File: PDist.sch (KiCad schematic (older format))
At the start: 2 parts

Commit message: Upgrade FPGA size, re-route SDRAM
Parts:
- removed BRIDGE1: XC6SLX25-CSG324, manuf:XILINX-CSG324, symbol XC6SLX25-CSG324
- added BRIDGE1: XC6SLX25-FGG484, manuf:XILINX-FGG484, symbol XC6SLX25-FGG484
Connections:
- net labels added: VCCAUX, VCORE
- net labels removed: +1.2, +3.3
- wire segments 150 -> 163

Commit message: Uh, more misc work.
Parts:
- added LIMB1: LPC435xFET256, smd-semi:BGA100P1700X1700-256, symbol LPC435xFET256
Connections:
- net labels added: 3V3_LIMB
- wire segments 163 -> 208
- no-connect marks 0 -> 1
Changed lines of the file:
@@
 $Descr A4 11693 8268
 encoding utf-8
-Sheet 3 8
+Sheet 3 9
 Title ""
 Date ""
@@
 Wire Wire Line
 	6000 6900 6000 1000
+$Comp
+L LPC435xFET256 LIMB?
+U 1 1 577B6870
+P 9400 4700
+AR Path="/5765CB89/577B6870" Ref="LIMB?"  Part="2"
+AR Path="/5763AB3B/577B6870" Ref="LIMB1"  Part="1"
+F 0 "LIMB1" H 10431 3696 50  0000 L CNN
+F 1 "LPC435xFET256" H 10431 3605 50  0000 L CNN
+F 2 "smd-semi:BGA100P1700X1700-256" H 9400 5200 50  0001 C CNN
+F 3 "http://www.nxp.com/documents/data_sheet/LPC435X_3X_2X_1X.pdf" H 9400 5100 50  0001 C CNN
+	1    9400 4700
+	1    0    0    -1
+$EndComp
+$Comp
+L GND #PWR6
+U 1 1 577B6906
+P 9300 6900
+F 0 "#PWR6" H 9300 6900 30  0001 C CNN
+F 1 "GND" H 9300 6830 30  0001 C CNN
+F 2 "" H 9300 6900 60  0000 C CNN
+F 3 "" H 9300 6900 60  0000 C CNN
+	1    9300 6900
+	1    0    0    -1
+$EndComp
+Wire Wire Line
+	9300 4700 9400 4700
+Wire Wire Line
+	9300 4800 9400 4800
+Wire Wire Line
+	9300 4900 9400 4900
+Wire Wire Line
+	9300 5000 9400 5000
+Wire Wire Line
+	9300 5100 9400 5100
+Wire Wire Line
+	9300 5200 9400 5200
+Wire Wire Line
+	9300 5300 9400 5300
+Wire Wire Line
+	9300 5400 9400 5400
+Wire Wire Line
+	9300 5500 9400 5500
+Wire Wire Line
+	9300 5600 9400 5600
+Wire Wire Line
+	9300 5700 9400 5700
+Wire Wire Line
+	9300 5800 9400 5800
+Wire Wire Line
+	9300 5900 9400 5900
+Wire Wire Line
+	9300 6000 9400 6000
+Wire Wire Line
+	9300 6100 9400 6100
+Wire Wire Line
+	9300 6200 9400 6200
+Wire Wire Line
+	9300 6300 9400 6300
+Wire Wire Line
+	9300 6400 9400 6400
+Wire Wire Line
+	9300 6500 9400 6500
+Wire Wire Line
+	9300 6600 9400 6600
+Wire Wire Line
+	9300 6700 9400 6700
+Wire Wire Line
+	9300 6800 9400 6800
+Connection ~ 9300 4800
+Connection ~ 9300 4900
+Connection ~ 9300 5000
+Connection ~ 9300 5100
+Connection ~ 9300 5200
+Connection ~ 9300 5300
+Connection ~ 9300 5400
+Connection ~ 9300 5500
+Connection ~ 9300 5600
+Connection ~ 9300 5700
+Connection ~ 9300 5800
+Connection ~ 9300 5900
+Connection ~ 9300 6000
+Connection ~ 9300 6100
+Connection ~ 9300 6200
+Connection ~ 9300 6300
+Connection ~ 9300 6400
+Connection ~ 9300 6500
+Connection ~ 9300 6600
+Connection ~ 9300 6700
+Connection ~ 9300 6800
+Wire Wire Line
+	9300 4700 9300 6900
+$Comp
+L LPC435xFET256 LIMB?
+U 19 1 577B6DFB
+P 9400 2300
+AR Path="/5765CB89/577B6DFB" Ref="LIMB?"  Part="2"
+AR Path="/5763AB3B/577B6DFB" Ref="LIMB1"  Part="19"
+F 0 "LIMB1" H 10631 1296 50  0000 L CNN
+F 1 "LPC435xFET256" H 10631 1205 50  0000 L CNN
+F 2 "smd-semi:BGA100P1700X1700-256" H 9400 2800 50  0001 C CNN
+F 3 "http://www.nxp.com/documents/data_sheet/LPC435X_3X_2X_1X.pdf" H 9400 2700 50  0001 C CNN
+	19   9400 2300
+	1    0    0    -1
+$EndComp
+Wire Wire Line
+	9200 2300 9400 2300
+Wire Wire Line
+	9300 2400 9400 2400
+Wire Wire Line
+	9300 2500 9400 2500
+Wire Wire Line
+	9300 2600 9400 2600
+Wire Wire Line
+	9300 2700 9400 2700
+Wire Wire Line
+	9300 2800 9400 2800
+Wire Wire Line
+	9300 3000 9400 3000
+Wire Wire Line
+	9300 3100 9400 3100
+Wire Wire Line
+	9300 3200 9400 3200
+Wire Wire Line
+	9300 3300 9400 3300
+Wire Wire Line
+	9300 3400 9400 3400
+Wire Wire Line
+	9300 3500 9400 3500
+Wire Wire Line
+	9300 3600 9400 3600
+Wire Wire Line
+	9300 3700 9400 3700
+Wire Wire Line
+	9300 3800 9400 3800
+Wire Wire Line
+	9300 3900 9400 3900
+Wire Wire Line
+	9300 4000 9400 4000
+Wire Wire Line
+	9300 4100 9400 4100
+Wire Wire Line
+	9300 4200 9400 4200
+Wire Wire Line
+	9300 4300 9400 4300
+Wire Wire Line
+	9300 4400 9400 4400
+Connection ~ 9300 2300
+Connection ~ 9300 2400
+Connection ~ 9300 2500
+Connection ~ 9300 2600
+Connection ~ 9300 2700
+Connection ~ 9300 2800
+Connection ~ 9300 3000
+Connection ~ 9300 3100
+Connection ~ 9300 3200
+Connection ~ 9300 3300
+Connection ~ 9300 3400
+Connection ~ 9300 3500
+Connection ~ 9300 3600
+Connection ~ 9300 3700
+Connection ~ 9300 3800
+Connection ~ 9300 3900
+Connection ~ 9300 4000
+Connection ~ 9300 4100
+Connection ~ 9300 4200
+Connection ~ 9300 4300
+NoConn ~ 9400 2900
+Text GLabel 9200 2300 0    50   Input ~ 0
+3V3_LIMB
+Wire Wire Line
+	9300 2300 9300 4400
 $EndSCHEMATC

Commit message: MOAR WORK
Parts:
- removed LIMB1: LPC435xFET256, smd-semi:BGA100P1700X1700-256, symbol LPC435xFET256
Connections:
- net labels removed: 3V3_LIMB
- wire segments 208 -> 163
- no-connect marks 1 -> 0
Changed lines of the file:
@@
 Wire Wire Line
 	6000 6900 6000 1000
-$Comp
-L LPC435xFET256 LIMB?
-U 1 1 577B6870
-P 9400 4700
-AR Path="/5765CB89/577B6870" Ref="LIMB?"  Part="2"
-AR Path="/5763AB3B/577B6870" Ref="LIMB1"  Part="1"
-F 0 "LIMB1" H 10431 3696 50  0000 L CNN
-F 1 "LPC435xFET256" H 10431 3605 50  0000 L CNN
-F 2 "smd-semi:BGA100P1700X1700-256" H 9400 5200 50  0001 C CNN
-F 3 "http://www.nxp.com/documents/data_sheet/LPC435X_3X_2X_1X.pdf" H 9400 5100 50  0001 C CNN
-	1    9400 4700
-	1    0    0    -1
-$EndComp
-$Comp
-L GND #PWR6
-U 1 1 577B6906
-P 9300 6900
-F 0 "#PWR6" H 9300 6900 30  0001 C CNN
-F 1 "GND" H 9300 6830 30  0001 C CNN
-F 2 "" H 9300 6900 60  0000 C CNN
-F 3 "" H 9300 6900 60  0000 C CNN
-	1    9300 6900
-	1    0    0    -1
-$EndComp
-Wire Wire Line
-	9300 4700 9400 4700
-Wire Wire Line
-	9300 4800 9400 4800
-Wire Wire Line
-	9300 4900 9400 4900
-Wire Wire Line
-	9300 5000 9400 5000
-Wire Wire Line
-	9300 5100 9400 5100
-Wire Wire Line
-	9300 5200 9400 5200
-Wire Wire Line
-	9300 5300 9400 5300
-Wire Wire Line
-	9300 5400 9400 5400
-Wire Wire Line
-	9300 5500 9400 5500
-Wire Wire Line
-	9300 5600 9400 5600
-Wire Wire Line
-	9300 5700 9400 5700
-Wire Wire Line
-	9300 5800 9400 5800
-Wire Wire Line
-	9300 5900 9400 5900
-Wire Wire Line
-	9300 6000 9400 6000
-Wire Wire Line
-	9300 6100 9400 6100
-Wire Wire Line
-	9300 6200 9400 6200
-Wire Wire Line
-	9300 6300 9400 6300
-Wire Wire Line
-	9300 6400 9400 6400
-Wire Wire Line
-	9300 6500 9400 6500
-Wire Wire Line
-	9300 6600 9400 6600
-Wire Wire Line
-	9300 6700 9400 6700
-Wire Wire Line
-	9300 6800 9400 6800
-Connection ~ 9300 4800
-Connection ~ 9300 4900
-Connection ~ 9300 5000
-Connection ~ 9300 5100
-Connection ~ 9300 5200
-Connection ~ 9300 5300
-Connection ~ 9300 5400
-Connection ~ 9300 5500
-Connection ~ 9300 5600
-Connection ~ 9300 5700
-Connection ~ 9300 5800
-Connection ~ 9300 5900
-Connection ~ 9300 6000
-Connection ~ 9300 6100
-Connection ~ 9300 6200
-Connection ~ 9300 6300
-Connection ~ 9300 6400
-Connection ~ 9300 6500
-Connection ~ 9300 6600
-Connection ~ 9300 6700
-Connection ~ 9300 6800
-Wire Wire Line
-	9300 4700 9300 6900
-$Comp
-L LPC435xFET256 LIMB?
-U 19 1 577B6DFB
-P 9400 2300
-AR Path="/5765CB89/577B6DFB" Ref="LIMB?"  Part="2"
-AR Path="/5763AB3B/577B6DFB" Ref="LIMB1"  Part="19"
-F 0 "LIMB1" H 10631 1296 50  0000 L CNN
-F 1 "LPC435xFET256" H 10631 1205 50  0000 L CNN
-F 2 "smd-semi:BGA100P1700X1700-256" H 9400 2800 50  0001 C CNN
-F 3 "http://www.nxp.com/documents/data_sheet/LPC435X_3X_2X_1X.pdf" H 9400 2700 50  0001 C CNN
-	19   9400 2300
-	1    0    0    -1
-$EndComp
-Wire Wire Line
-	9200 2300 9400 2300
-Wire Wire Line
-	9300 2400 9400 2400
-Wire Wire Line
-	9300 2500 9400 2500
-Wire Wire Line
-	9300 2600 9400 2600
-Wire Wire Line
-	9300 2700 9400 2700
-Wire Wire Line
-	9300 2800 9400 2800
-Wire Wire Line
-	9300 3000 9400 3000
-Wire Wire Line
-	9300 3100 9400 3100
-Wire Wire Line
-	9300 3200 9400 3200
-Wire Wire Line
-	9300 3300 9400 3300
-Wire Wire Line
-	9300 3400 9400 3400
-Wire Wire Line
-	9300 3500 9400 3500
-Wire Wire Line
-	9300 3600 9400 3600
-Wire Wire Line
-	9300 3700 9400 3700
-Wire Wire Line
-	9300 3800 9400 3800
-Wire Wire Line
-	9300 3900 9400 3900
-Wire Wire Line
-	9300 4000 9400 4000
-Wire Wire Line
-	9300 4100 9400 4100
-Wire Wire Line
-	9300 4200 9400 4200
-Wire Wire Line
-	9300 4300 9400 4300
-Wire Wire Line
-	9300 4400 9400 4400
-Connection ~ 9300 2300
-Connection ~ 9300 2400
-Connection ~ 9300 2500
-Connection ~ 9300 2600
-Connection ~ 9300 2700
-Connection ~ 9300 2800
-Connection ~ 9300 3000
-Connection ~ 9300 3100
-Connection ~ 9300 3200
-Connection ~ 9300 3300
-Connection ~ 9300 3400
-Connection ~ 9300 3500
-Connection ~ 9300 3600
-Connection ~ 9300 3700
-Connection ~ 9300 3800
-Connection ~ 9300 3900
-Connection ~ 9300 4000
-Connection ~ 9300 4100
-Connection ~ 9300 4200
-Connection ~ 9300 4300
-NoConn ~ 9400 2900
-Text GLabel 9200 2300 0    50   Input ~ 0
-3V3_LIMB
-Wire Wire Line
-	9300 2300 9300 4400
 $EndSCHEMATC

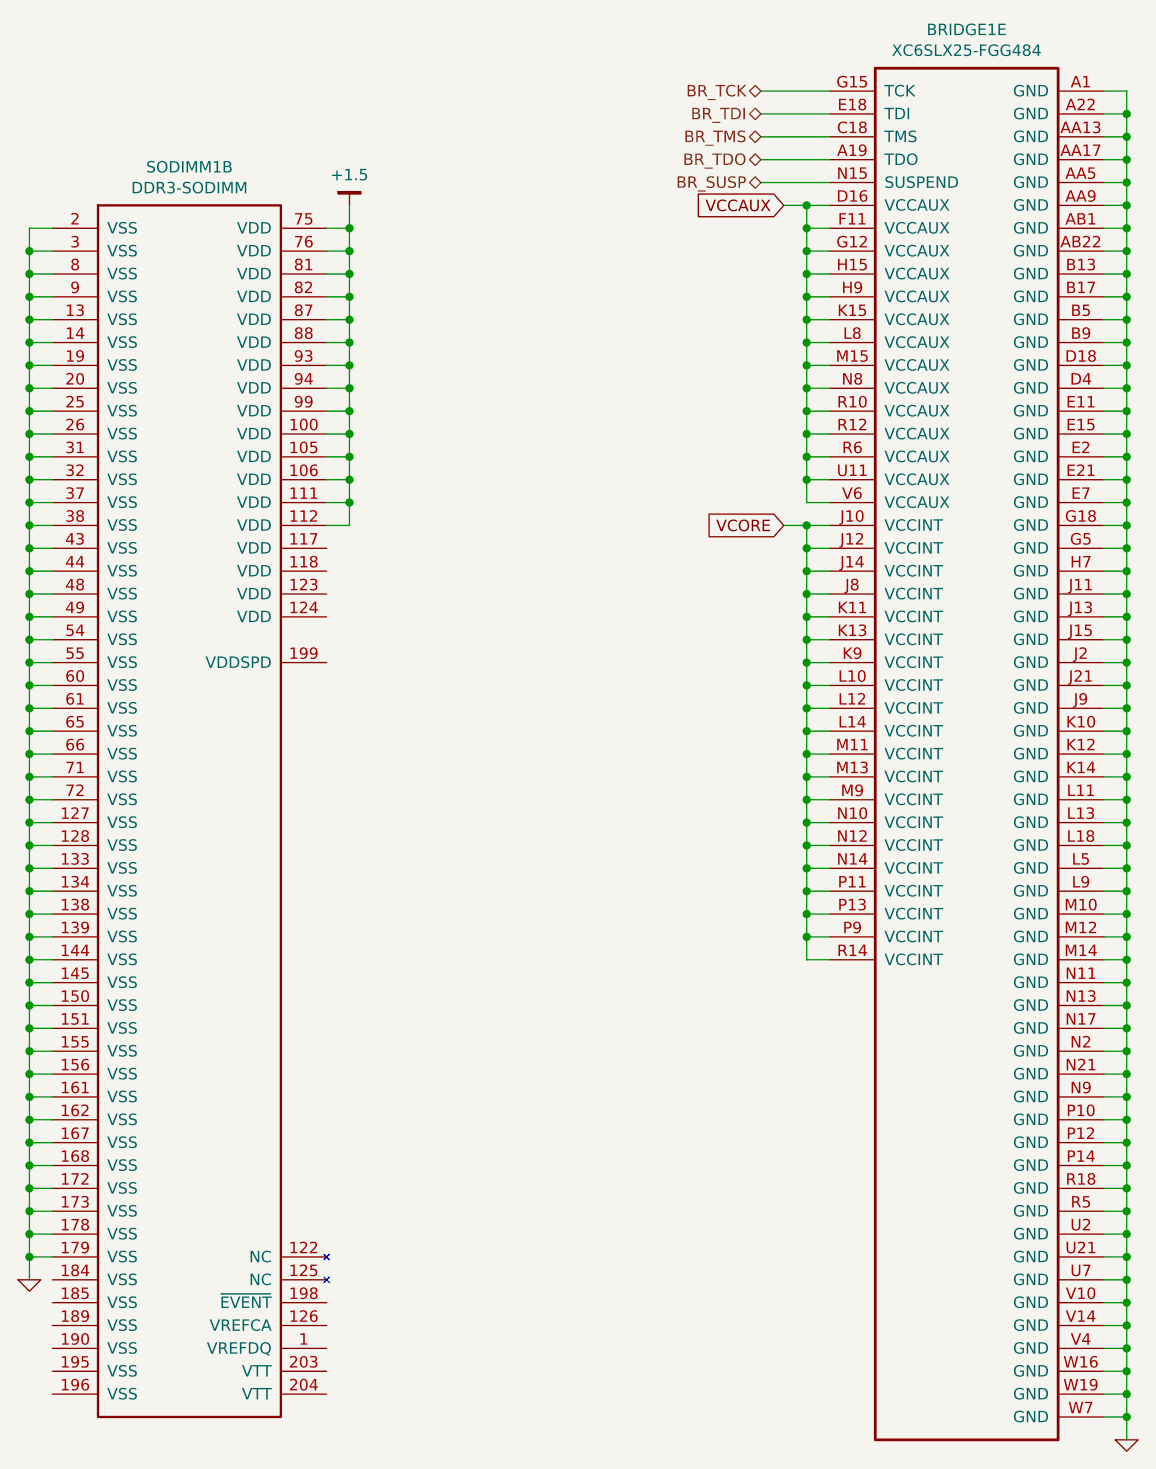
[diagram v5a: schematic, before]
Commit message: Rip up SDRAM and rotate FPGA
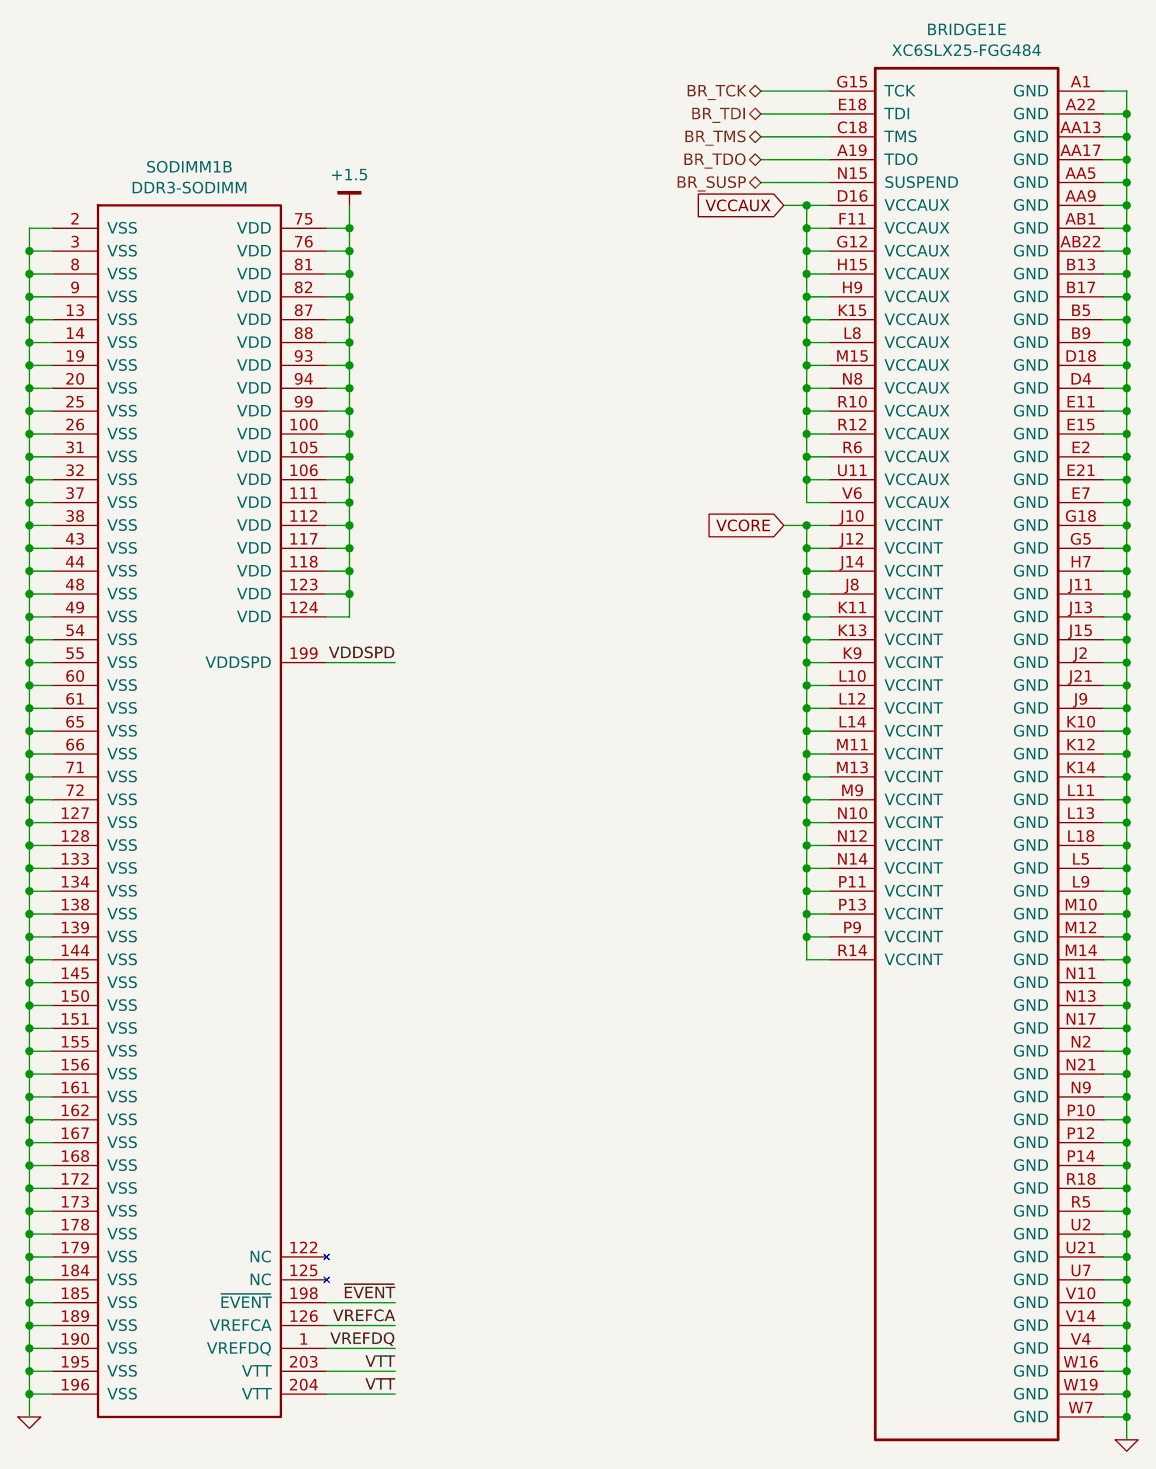
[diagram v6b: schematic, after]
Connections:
- net +1.5: now also SODIMM1.117 (VDD), SODIMM1.118 (VDD), SODIMM1.123 (VDD), SODIMM1.124 (VDD)
- net GND: now also SODIMM1.184 (VSS), SODIMM1.185 (VSS), SODIMM1.189 (VSS), SODIMM1.190 (VSS), SODIMM1.195 (VSS), SODIMM1.196 (VSS)
- net VREFDQ: now reaches SODIMM1.1 (VREFDQ)
- net VREFCA: now reaches SODIMM1.126 (VREFCA)
- net ~EVENT: now reaches SODIMM1.198 (~EVENT)
- net VDDSPD: now reaches SODIMM1.199 (VDDSPD)
- net VTT: now reaches SODIMM1.203 (VTT)
- net VTT: now also SODIMM1.204 (VTT)
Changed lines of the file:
@@
 $Descr A4 11693 8268
 encoding utf-8
-Sheet 3 9
+Sheet 3 10
 Title ""
 Date ""
@@
 L GND #PWR3
 U 1 1 57647804
-P 1200 6200
-F 0 "#PWR3" H 1200 6200 30  0001 C CNN
-F 1 "GND" H 1200 6130 30  0001 C CNN
-F 2 "" H 1200 6200 60  0000 C CNN
-F 3 "" H 1200 6200 60  0000 C CNN
-	1    1200 6200
+P 1200 6800
+F 0 "#PWR3" H 1200 6800 30  0001 C CNN
+F 1 "GND" H 1200 6730 30  0001 C CNN
+F 2 "" H 1200 6800 60  0000 C CNN
+F 3 "" H 1200 6800 60  0000 C CNN
+	1    1200 6800
 	1    0    0    -1
 $EndComp
@@
 Connection ~ 1200 6100
 Wire Wire Line
-	1200 1600 1200 6200
+	1200 1600 1200 6800
 Wire Wire Line
 	2600 1600 2500 1600
@@
 Connection ~ 2600 2800
 Wire Wire Line
-	2600 1500 2600 2900
+	2600 1500 2600 3300
 Text HLabel 4400 1000 0    50   BiDi ~ 0
 BR_TCK
@@
 Connection ~ 4600 4700
 Wire Wire Line
-	4600 2800 4600 1500
+	4600 1500 4600 2800
 Text GLabel 4500 2900 0    50   Input ~ 0
 VCORE
 Wire Wire Line
-	4600 4800 4600 2900
+	4600 2900 4600 4800
 Wire Wire Line
 	6000 1000 5900 1000
@@
 Connection ~ 6000 6800
 Wire Wire Line
-	6000 6900 6000 1000
+	6000 1000 6000 6900
+Text Label 2800 6500 2    50   ~ 0
+VREFDQ
+Wire Wire Line
+	2800 6500 2500 6500
+Text Label 2800 3500 2    50   ~ 0
+VDDSPD
+Wire Wire Line
+	2800 3500 2500 3500
+Text Label 2800 6600 2    50   ~ 0
+VTT
+Text Label 2800 6700 2    50   ~ 0
+VTT
+Wire Wire Line
+	2800 6600 2500 6600
+Wire Wire Line
+	2800 6700 2500 6700
+Wire Wire Line
+	1300 6200 1200 6200
+Connection ~ 1200 6200
+Wire Wire Line
+	1300 6300 1200 6300
+Connection ~ 1200 6300
+Wire Wire Line
+	1300 6400 1200 6400
+Connection ~ 1200 6400
+Wire Wire Line
+	1300 6500 1200 6500
+Connection ~ 1200 6500
+Wire Wire Line
+	1300 6600 1200 6600
+Connection ~ 1200 6600
+Wire Wire Line
+	1300 6700 1200 6700
+Connection ~ 1200 6700
+Text Label 2800 6400 2    50   ~ 0
+VREFCA
+Wire Wire Line
+	2800 6400 2500 6400
+Text Label 2800 6300 2    50   ~ 0
+~EVENT
+Wire Wire Line
+	2800 6300 2500 6300
+Wire Wire Line
+	2600 3000 2500 3000
+Connection ~ 2600 2900
+Wire Wire Line
+	2600 3100 2500 3100
+Connection ~ 2600 3000
+Wire Wire Line
+	2600 3200 2500 3200
+Connection ~ 2600 3100
+Wire Wire Line
+	2600 3300 2500 3300
+Connection ~ 2600 3200
 $EndSCHEMATC
